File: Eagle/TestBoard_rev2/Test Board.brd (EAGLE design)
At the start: 38.1 x 38.1 mm, 13 parts

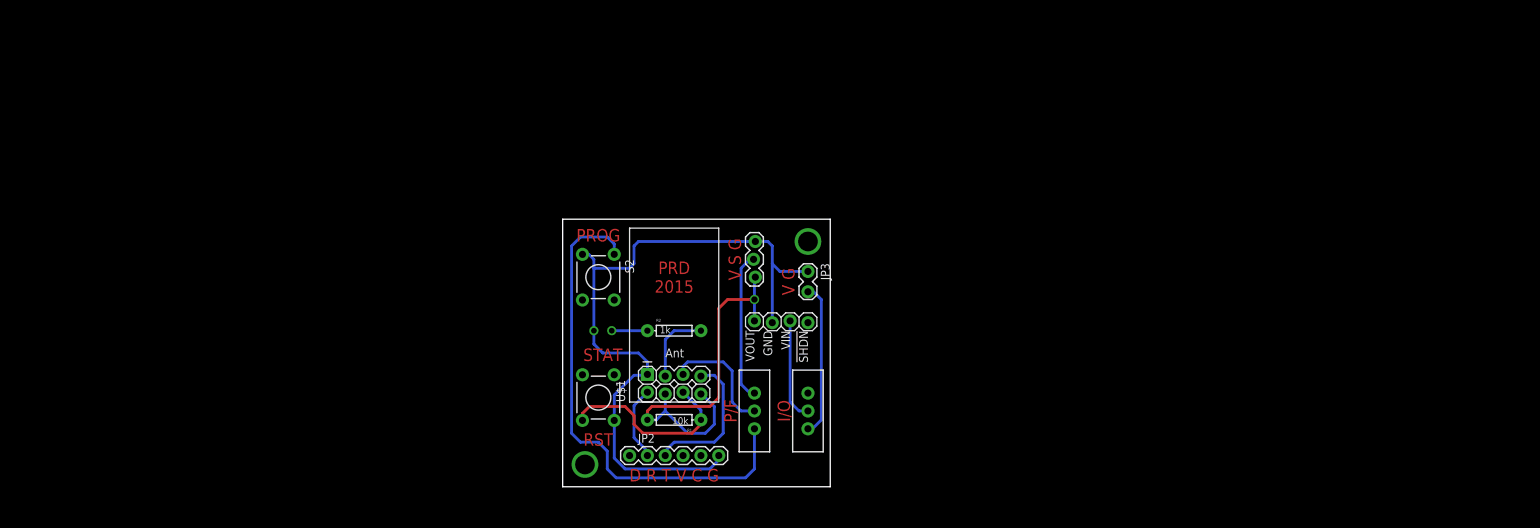
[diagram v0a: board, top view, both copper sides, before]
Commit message: Added Rev2 of the prototype PCB
Added a second revision that has a better form factor that can be better
mounted on the Flow sensor. The board needs to be laid out and there are
some design decisions that also need to be made.
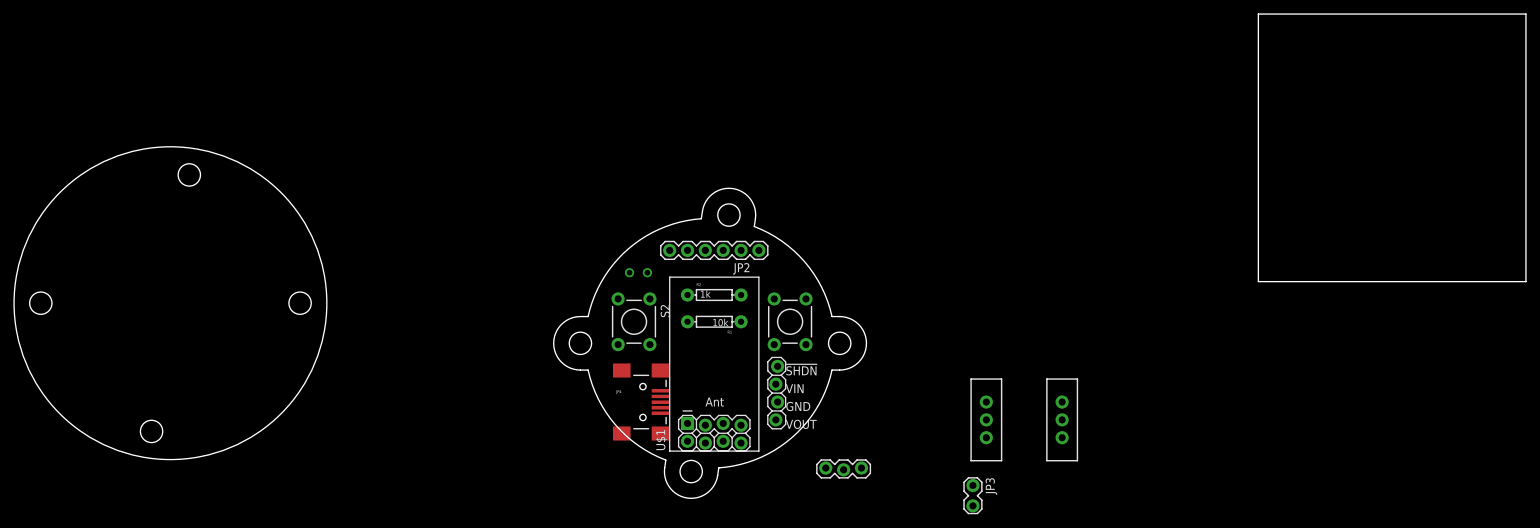
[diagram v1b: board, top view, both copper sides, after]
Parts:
- added JP4: USBSMD, SparkFun-Connectors:USB-MINIB
- moved JP3 38.5 mm to (58.4, 0.00)
- moved S4 36.2 mm to (71.1, 9.53)
- moved JP2 34.5 mm to (27.9, 33.7), turned to 180 degrees
- moved JP1 33.9 mm to (37.5, 2.54), turned to 0 degrees
- moved S1 33.0 mm to (60.3, 9.53)
- moved S3 29.4 mm to (32.4, 23.5)
- moved R1 15.1 mm to (21.6, 23.5)
- moved U$2 14.3 mm to (30.5, 9.53), turned to 90 degrees
- moved LED1 9.69 mm to (10.8, 30.5)
- moved U$1 9.03 mm to (15.2, 5.08)
- moved S2 8.13 mm to (10.2, 23.5)
- moved R2 7.65 mm to (21.6, 27.3)
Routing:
- net GND: track 101.9 -> 0.00 mm
- net N$1: track 71.5 -> 0.00 mm
- net 3.3V: track 56.3 -> 0.00 mm, vias 1 -> 0
- net N$3: track 26.7 -> 0.00 mm
- net VIN: track 21.9 -> 0.00 mm
- net FLOW: track 21.2 -> 0.00 mm
- net N$4: track 20.7 -> 0.00 mm
- net N$7: track 17.1 -> 0.00 mm
- net N$8: track 14.6 -> 0.00 mm
- net N$6: track 10.8 -> 0.00 mm
- net N$2: track 10.6 -> 0.00 mm
- net N$5: track 5.08 -> 0.00 mm
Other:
- board size 38.1 x 38.1 mm -> 215.3 x 69 mm
- board text removed: "D R T V C G"
- board text removed: "I/O"
- board text removed: "P/F"
- board text removed: "PRD 2015"
- board text removed: "PROG"
- board text removed: "RST"
- board text removed: "STAT"
- board text removed: "V G"
- board text removed: "V S G"
